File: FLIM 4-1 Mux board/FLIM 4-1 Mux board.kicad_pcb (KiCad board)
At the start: 4 copper layers, 74.5 x 100 mm, 66 parts, among them J1 Barrel_Jack, J2 RJ45_Shielded, J3 Conn_Coaxial, J4 Conn_Coaxial, J5 Conn_Coaxial, J6 Conn_Coaxial, J7 Conn_Coaxial, U1 ADM7150ARDZ-5.0, U2 74AHCT74D_118, U3 74AHCT74D_118, U4 SPDT RF switch, U5 SPDT RF switch, U6 SPDT RF switch

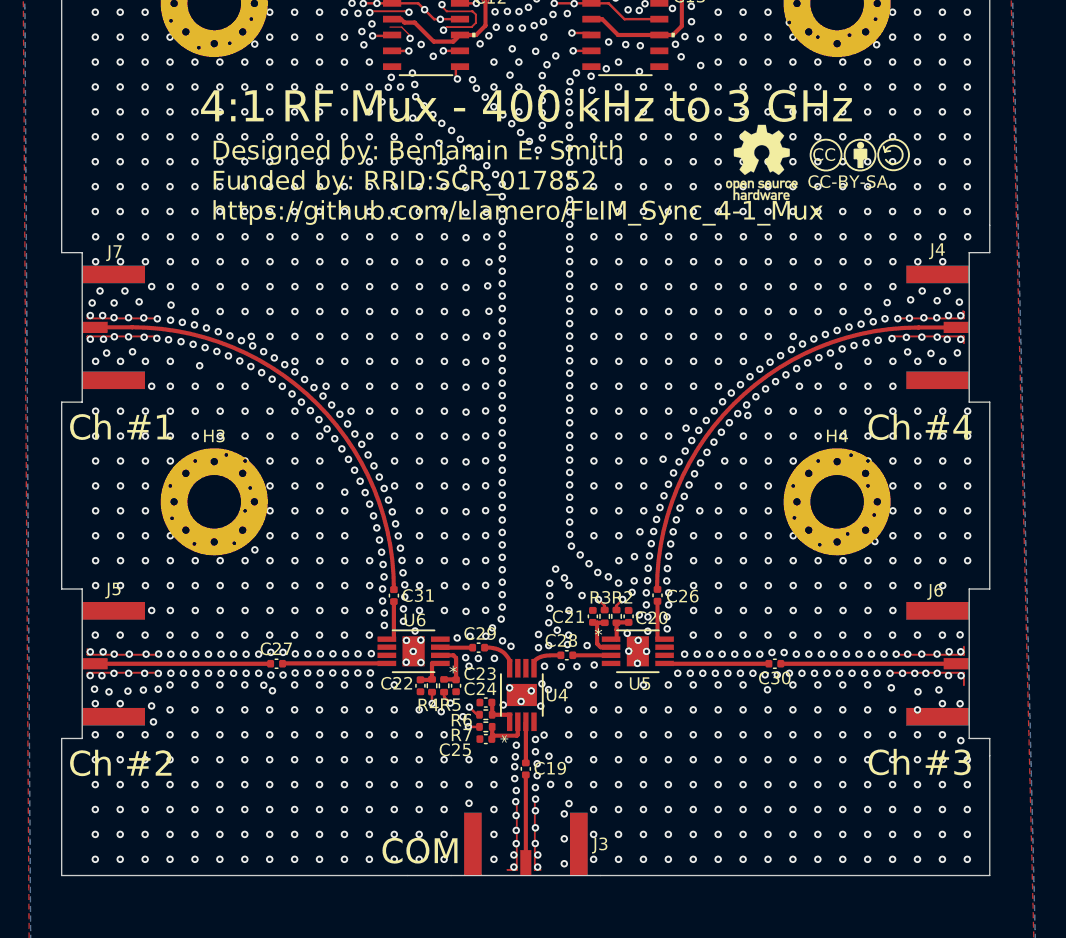
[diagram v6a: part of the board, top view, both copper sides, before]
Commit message: Add vias to SMA GND pads, pulls guards to vertex of SMA transition
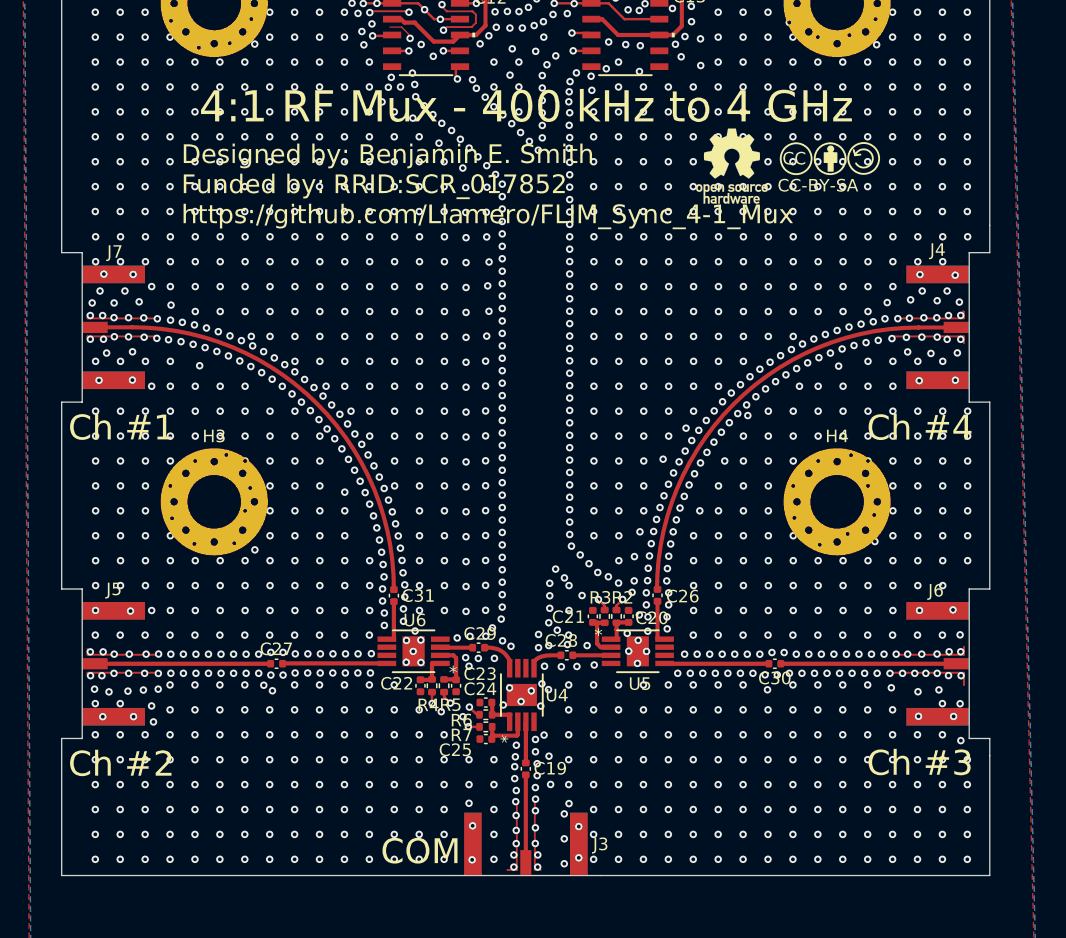
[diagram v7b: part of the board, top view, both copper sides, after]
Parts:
- moved SYM1 2.42 mm to (116.5, 83.0)
- moved SYM2 2.42 mm to (124.6, 82.2)
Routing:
- net GND: vias 1923 -> 1942
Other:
- board text added: "4:1 RF Mux - 400 kHz to 4 GHz"
- board text removed: "4:1 RF Mux - 400 kHz to 3 GHz"
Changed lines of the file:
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@@
 	(footprint "Symbol:OSHW-Logo_5.7x6mm_SilkScreen"
 		(layer "F.Cu")
-		(at 118.95 82.76)
+		(at 116.55 83.05)
 		(descr "Open Source Hardware Logo")
 		(tags "Logo OSHW")
@@
 	(footprint "Custom:CC-BY-SA Symbol"
 		(layer "F.Cu")
-		(at 126.97 81.92)
+		(at 124.57 82.21)
 		(descr "Symbol, Creative Commons Public Domain, SilkScreenTop, Small,")
 		(tags "Symbol, Creative Commons Public Domain, SilkScreen Top, Small,")
@@
 	)
 	(gr_text "Designed by: Benjamin E. Smith\nFunded by: RRID:SCR_017852\nhttps://github.com/Llamero/FLIM_Sync_4-1_Mux"
-		(at 74.75 87.53 0)
+		(at 72.35 87.82 0)
 		(layer "F.SilkS")
 		(effects
@@
 		)
 	)
-	(gr_text "4:1 RF Mux - 400 kHz to 3 GHz"
+	(gr_text "4:1 RF Mux - 400 kHz to 4 GHz"
 		(at 100.05 79.77 0)
 		(layer "F.SilkS")
@@
 	)
 	(via
+		(at 68.49 91.75)
+		(size 0.6)
+		(drill 0.3)
+		(layers "F.Cu" "B.Cu")
+		(net "GND")
+	)
+	(via
 		(at 89.9505 76.7005)
 		(size 0.6)
@@
 	)
 	(via
+		(at 95.74 136.01)
+		(size 0.6)
+		(drill 0.3)
+		(layers "F.Cu" "B.Cu")
+		(net "GND")
+	)
+	(via
 		(at 125.745 122.23275)
 		(size 0.6)
@@
 	)
 	(via
+		(at 104.26 138.58)
+		(size 0.6)
+		(drill 0.3)
+		(layers "F.Cu" "B.Cu")
+		(net "GND")
+	)
+	(via
 		(at 107.453827 116.523877)
 		(size 0.6)
@@
 	)
 	(via
-		(at 134.92 95.06)
+		(at 134.92 95.04)
 		(size 0.6)
 		(drill 0.3)
@@
 	)
 	(via
+		(at 131.59 100.28)
+		(size 0.6)
+		(drill 0.3)
+		(layers "F.Cu" "B.Cu")
+		(net "GND")
+	)
+	(via
 		(at 99.23 135.18)
 		(size 0.6)
@@
 	)
 	(via
+		(at 66.05 127.25)
+		(size 0.6)
+		(drill 0.3)
+		(layers "F.Cu" "B.Cu")
+		(net "GND")
+	)
+	(via
 		(at 97.05 94.71)
 		(size 0.6)
@@
 	)
 	(via
+		(at 65.47 118.72)
+		(size 0.6)
+		(drill 0.3)
+		(layers "F.Cu" "B.Cu")
+		(net "GND")
+	)
+	(via
 		(at 90.071719 114.709249)
 		(size 0.6)
@@
 	)
 	(via
+		(at 134.3 118.68)
+		(size 0.6)
+		(drill 0.3)
+		(layers "F.Cu" "B.Cu")
+		(net "GND")
+	)
+	(via
 		(at 65.4505 60.7005)
 		(size 0.6)
@@
 	)
 	(via
+		(at 68.28 118.77)
+		(size 0.6)
+		(drill 0.3)
+		(layers "F.Cu" "B.Cu")
+		(net "GND")
+	)
+	(via
 		(at 115.4505 54.7005)
 		(size 0.6)
@@
 	)
 	(via
+		(at 65.75 100.25)
+		(size 0.6)
+		(drill 0.3)
+		(layers "F.Cu" "B.Cu")
+		(net "GND")
+	)
+	(via
 		(at 106.55 52.6)
 		(size 0.6)
@@
 	)
 	(via
+		(at 104.26 136.07)
+		(size 0.6)
+		(drill 0.3)
+		(layers "F.Cu" "B.Cu")
+		(net "GND")
+	)
+	(via
 		(at 113.4755 64.7255)
 		(size 0.6)
@@
 	)
 	(via
+		(at 134.35 127.23)
+		(size 0.6)
+		(drill 0.3)
+		(layers "F.Cu" "B.Cu")
+		(net "GND")
+	)
+	(via
 		(at 109.4755 64.7255)
 		(size 0.6)
@@
 	)
 	(via
+		(at 131.61 118.72)
+		(size 0.6)
+		(drill 0.3)
+		(layers "F.Cu" "B.Cu")
+		(net "GND")
+	)
+	(via
 		(at 125.4505 62.7005)
 		(size 0.6)
@@
 	)
 	(via
-		(at 65.04 123.95)
+		(at 65.07 123.96)
 		(size 0.6)
 		(drill 0.3)
@@
 	)
 	(via
+		(at 66.14 91.72)
+		(size 0.6)
+		(drill 0.3)
+		(layers "F.Cu" "B.Cu")
+		(net "GND")
+	)
+	(via
 		(at 79.4505 68.7005)
 		(size 0.6)
@@
 	)
 	(via
+		(at 134.49 100.24)
+		(size 0.6)
+		(drill 0.3)
+		(layers "F.Cu" "B.Cu")
+		(net "GND")
+	)
+	(via
 		(at 127.4755 102.7255)
 		(size 0.6)
@@
 	)
 	(via
+		(at 68.43 100.23)
+		(size 0.6)
+		(drill 0.3)
+		(layers "F.Cu" "B.Cu")
+		(net "GND")
+	)
+	(via
 		(at 91.4755 114.7255)
 		(size 0.6)
@@
 	)
 	(via
+		(at 131.65 91.76)
+		(size 0.6)
+		(drill 0.3)
+		(layers "F.Cu" "B.Cu")
+		(net "GND")
+	)
+	(via
 		(at 125.4505 120.7005)
 		(size 0.6)
@@
 	)
 	(via
-		(at 131.4505 126.7005)
+		(at 131.53 127.22)
 		(size 0.6)
 		(drill 0.3)
@@
 	)
 	(via
+		(at 95.7 138.74)
+		(size 0.6)
+		(drill 0.3)
+		(layers "F.Cu" "B.Cu")
+		(net "GND")
+	)
+	(via
 		(at 111.4755 88.7255)
 		(size 0.6)
@@
 	)
 	(via
+		(at 68.52 127.25)
+		(size 0.6)
+		(drill 0.3)
+		(layers "F.Cu" "B.Cu")
+		(net "GND")
+	)
+	(via
 		(at 100.3 63.64)
 		(size 0.6)
@@
 	)
 	(via
+		(at 134.48 91.81)
+		(size 0.6)
+		(drill 0.3)
+		(layers "F.Cu" "B.Cu")
+		(net "GND")
+	)
+	(via
 		(at 131.4755 104.7255)
 		(size 0.6)
@@
 		)
 	)
+	(group ""
+		(members "2dd2cfad-fd11-4274-a2c9-eefdc360f8da" "40d07f3d-d163-4b89-ad4d-818c59789f29"
+			"c36aa290-a7bf-45e7-a6ba-6573051508d6"
+		)
+	)

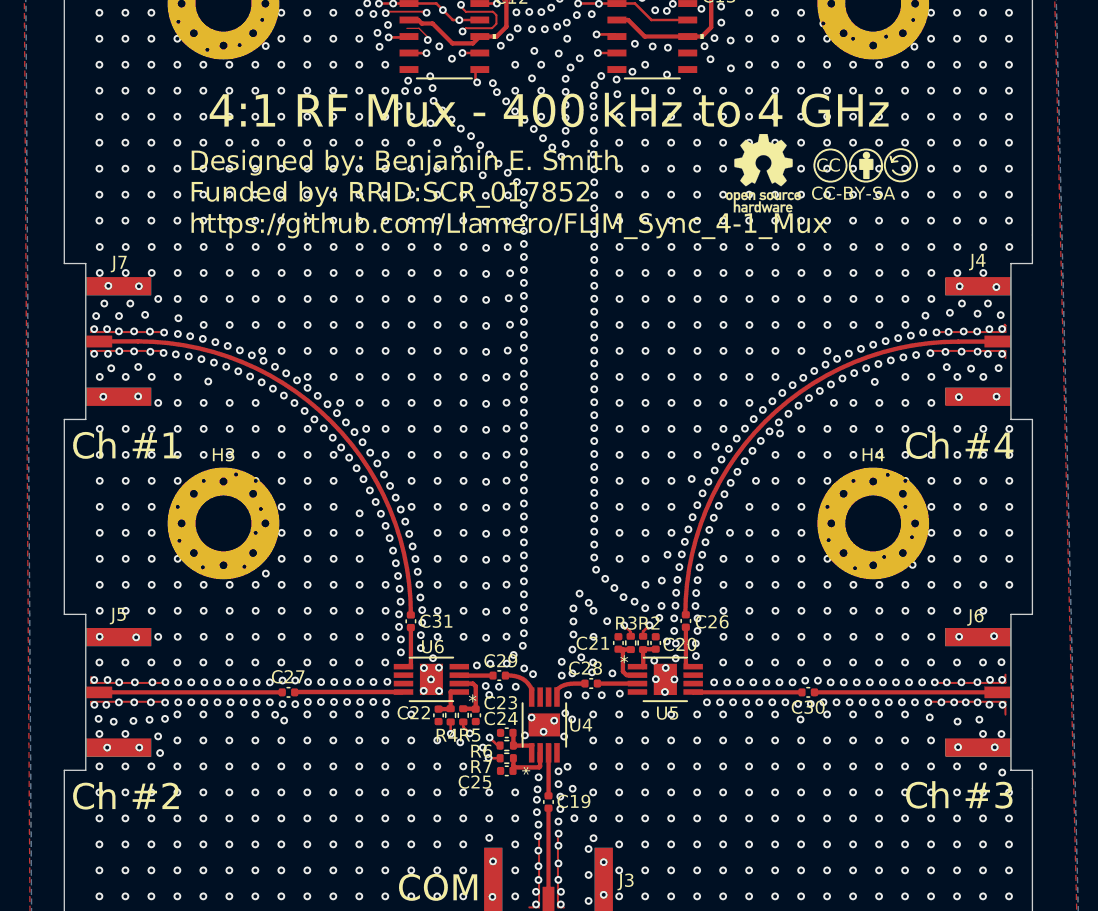
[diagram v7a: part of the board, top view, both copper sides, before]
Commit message: Switch to 100 nF 0201 RF caps for waveguides
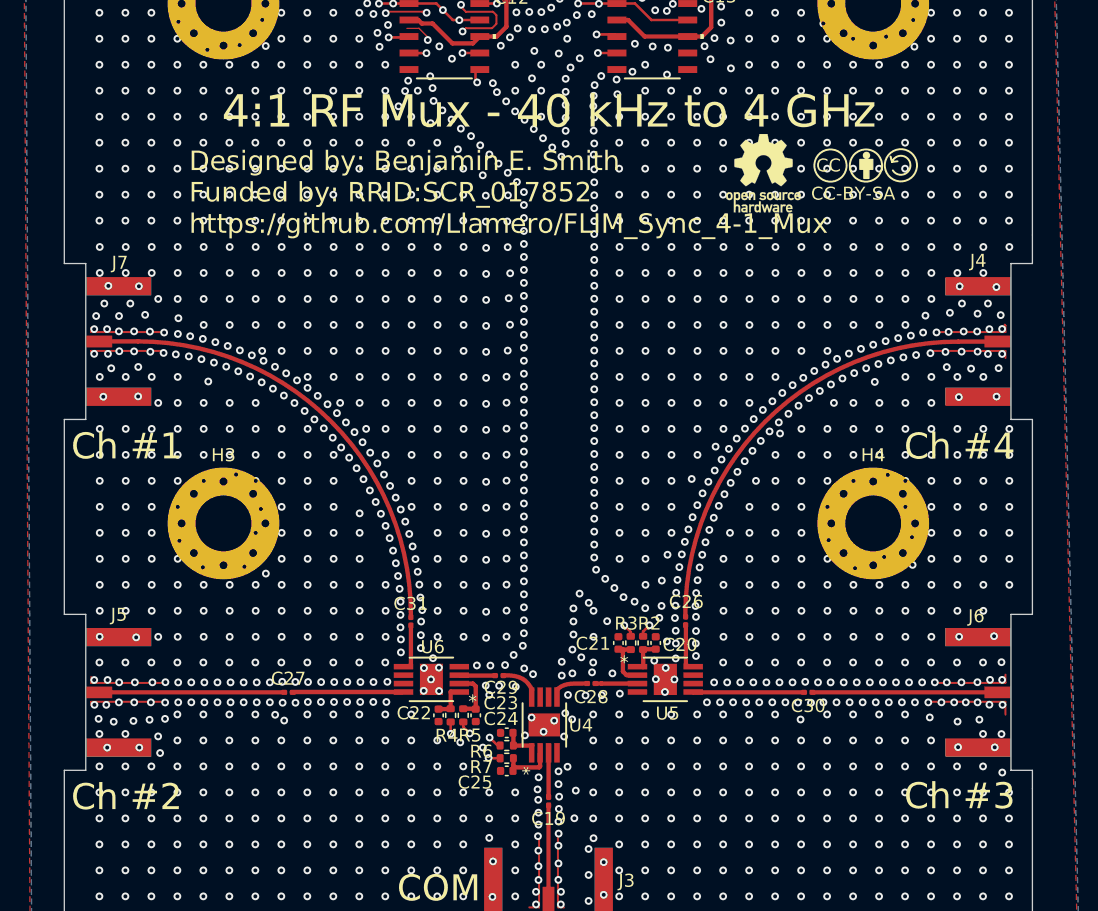
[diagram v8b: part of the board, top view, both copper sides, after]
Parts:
- C19, C26, C27, C28, C29, C30, C31: value 8.2 nF -> 100 nF; footprint Capacitor_SMD:C_0402_1005Metric -> Capacitor_SMD:C_0201_0603Metric
- moved C19 0.06 mm to (100.0, 131.4), turned to -90 degrees
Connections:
- C19 pad 1: Net-(J3-In) -> Net-(U4-RFC)
- C19 pad 2: Net-(U4-RFC) -> Net-(J3-In)
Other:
- board text added: "4:1 RF Mux - 40 kHz to 4 GHz"
- board text removed: "4:1 RF Mux - 400 kHz to 4 GHz"
